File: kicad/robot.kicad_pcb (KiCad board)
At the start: 2 copper layers, 67.6 x 59.8 mm, 67 parts, among them J1 Adafruit Coil Jumper, J2 Adafruit Coil Jumper, J3 Adafruit Coil Jumper, J4 Adafruit Coil Jumper, M5 Motor_DC, M6 Motor_DC, M7 Motor_DC, M8 Motor_DC, Q2 NMOS, U10 GY-521, U13 DRV8833PW, U6 DRV8833PW, U8 ESP32-DEVKITC, U9 MCP73831-2-OT

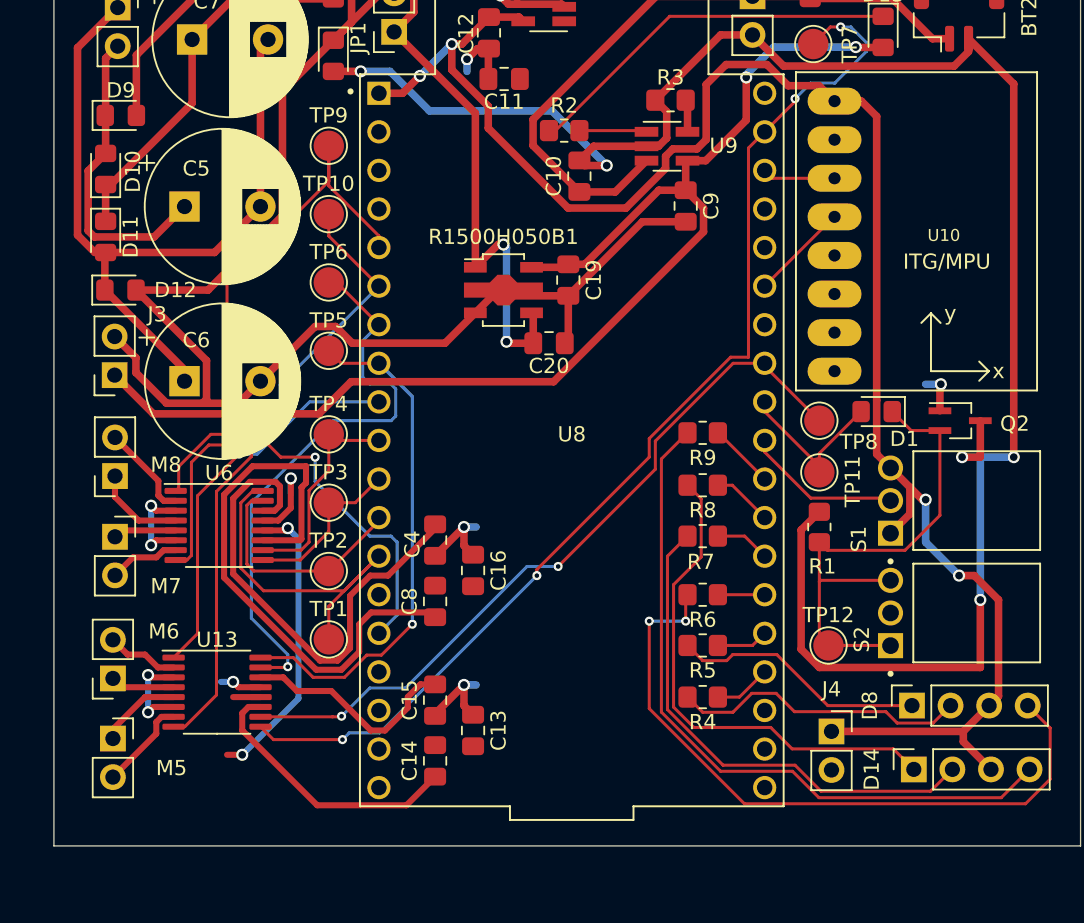
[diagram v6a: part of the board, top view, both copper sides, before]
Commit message: Add mounting holes
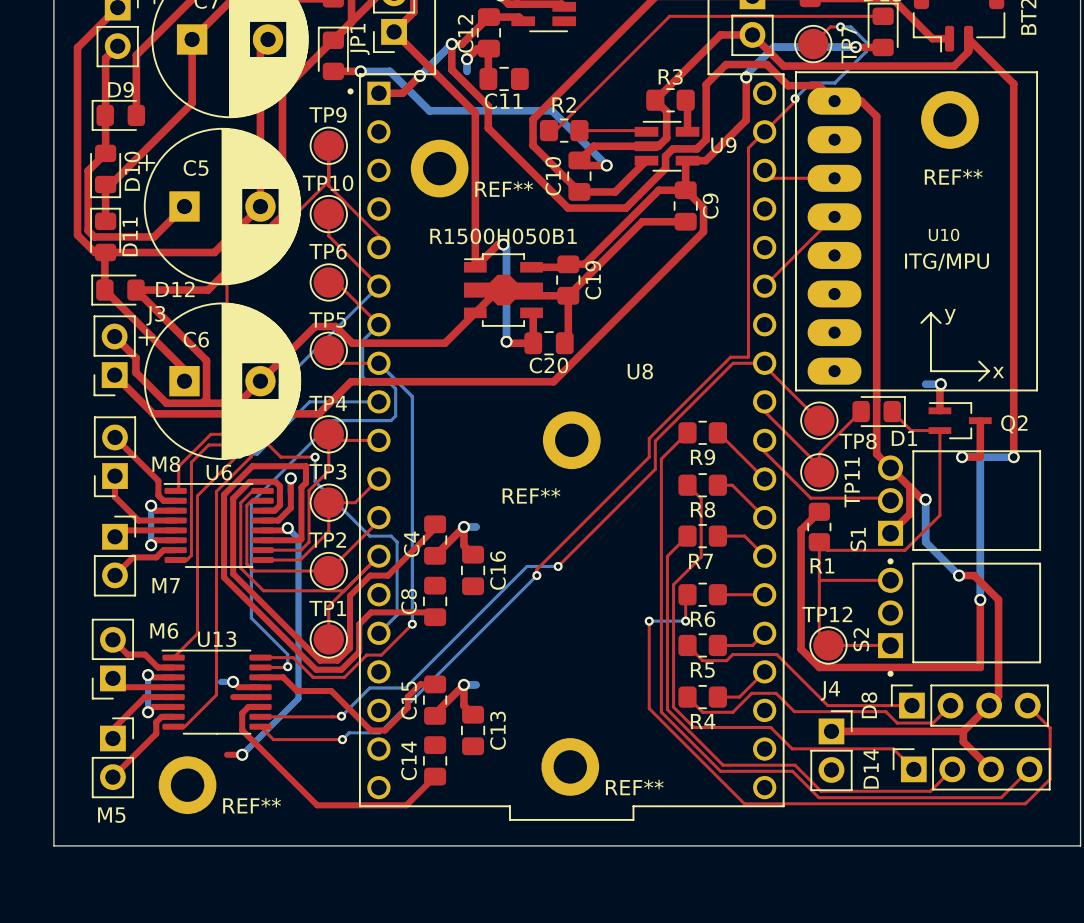
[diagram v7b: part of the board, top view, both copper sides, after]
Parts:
- added REF**: MountingHole_2.2mm_M2_DIN965_Pad, MountingHole:MountingHole_2.2mm_M2_DIN965_Pad, F.Cu at (181.8, 71.0)
- added REF**: MountingHole_2.2mm_M2_DIN965_Pad, MountingHole:MountingHole_2.2mm_M2_DIN965_Pad, F.Cu at (190.4, 110.4)
- added REF**: MountingHole_2.2mm_M2_DIN965_Pad, MountingHole:MountingHole_2.2mm_M2_DIN965_Pad, F.Cu at (215.4, 67.8)
- added REF**: MountingHole_2.2mm_M2_DIN965_Pad, MountingHole:MountingHole_2.2mm_M2_DIN965_Pad, F.Cu at (165.2, 111.6)
- added REF**: MountingHole_2.2mm_M2_DIN965_Pad, MountingHole:MountingHole_2.2mm_M2_DIN965_Pad, F.Cu at (190.5, 88.9)
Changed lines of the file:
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@@
       (net 39 "Net-(U13-nFAULT)") (pinfunction "1") (pintype "passive"))
   )
+  (footprint "MountingHole:MountingHole_2.2mm_M2_DIN965_Pad" (layer "F.Cu")
+    (at 181.8 71)
+    (descr "Mounting Hole 2.2mm, M2, DIN965")
+    (tags "mounting hole 2.2mm m2 din965")
+    (attr exclude_from_pos_files exclude_from_bom)
+    (fp_text reference "REF**" (at 4.2 1.4) (layer "F.SilkS")
+        (effects (font (size 1 1) (thickness 0.15)))
+    )
+    (fp_text value "MountingHole_2.2mm_M2_DIN965_Pad" (at 0 2.9) (layer "F.Fab")
+        (effects (font (size 1 1) (thickness 0.15)))
+    )
+    (fp_text user "${REFERENCE}" (at 0 0) (layer "F.Fab")
+        (effects (font (size 1 1) (thickness 0.15)))
+    )
+    (fp_circle (center 0 0) (end 1.9 0)
+      (stroke (width 0.15) (type solid)) (fill none) (layer "Cmts.User"))
+    (fp_circle (center 0 0) (end 2.15 0)
+      (stroke (width 0.05) (type solid)) (fill none) (layer "F.CrtYd"))
+    (pad "1" thru_hole circle (at 0 0) (size 3.8 3.8) (drill 2.2) (layers "*.Cu" "*.Mask"))
+  )
   (footprint "Connector_PinSocket_2.54mm:PinSocket_1x02_P2.54mm_Vertical" (layer "F.Cu")
     (at 160.6 60.4)
@@
     )
   )
+  (footprint "MountingHole:MountingHole_2.2mm_M2_DIN965_Pad" (layer "F.Cu")
+    (at 190.4 110.4)
+    (descr "Mounting Hole 2.2mm, M2, DIN965")
+    (tags "mounting hole 2.2mm m2 din965")
+    (attr exclude_from_pos_files exclude_from_bom)
+    (fp_text reference "REF**" (at 4.2 1.4) (layer "F.SilkS")
+        (effects (font (size 1 1) (thickness 0.15)))
+    )
+    (fp_text value "MountingHole_2.2mm_M2_DIN965_Pad" (at 0 2.9) (layer "F.Fab")
+        (effects (font (size 1 1) (thickness 0.15)))
+    )
+    (fp_text user "${REFERENCE}" (at 0 0) (layer "F.Fab")
+        (effects (font (size 1 1) (thickness 0.15)))
+    )
+    (fp_circle (center 0 0) (end 1.9 0)
+      (stroke (width 0.15) (type solid)) (fill none) (layer "Cmts.User"))
+    (fp_circle (center 0 0) (end 2.15 0)
+      (stroke (width 0.05) (type solid)) (fill none) (layer "F.CrtYd"))
+    (pad "1" thru_hole circle (at 0 0) (size 3.8 3.8) (drill 2.2) (layers "*.Cu" "*.Mask"))
+  )
   (footprint "Connector_PinSocket_2.54mm:PinSocket_1x02_P2.54mm_Vertical" (layer "F.Cu")
     (at 160.285 104.57 180)
@@
     (property "ki_keywords" "DC Motor")
     (attr through_hole)
-    (fp_text reference "M5" (at 3.8575 1.945) (layer "F.SilkS")
+    (fp_text reference "M5" (at -0.085 5.07) (layer "F.SilkS")
         (effects (font (size 1 1) (thickness 0.15)))
     )
@@
       (net 35 "Net-(U6-BIN2)") (pinfunction "1") (pintype "passive"))
   )
+  (footprint "MountingHole:MountingHole_2.2mm_M2_DIN965_Pad" (layer "F.Cu")
+    (at 215.4 67.8)
+    (descr "Mounting Hole 2.2mm, M2, DIN965")
+    (tags "mounting hole 2.2mm m2 din965")
+    (attr exclude_from_pos_files exclude_from_bom)
+    (fp_text reference "REF**" (at 0.2 3.8) (layer "F.SilkS")
+        (effects (font (size 1 1) (thickness 0.15)))
+    )
+    (fp_text value "MountingHole_2.2mm_M2_DIN965_Pad" (at 0 2.9) (layer "F.Fab")
+        (effects (font (size 1 1) (thickness 0.15)))
+    )
+    (fp_text user "${REFERENCE}" (at 0 0) (layer "F.Fab")
+        (effects (font (size 1 1) (thickness 0.15)))
+    )
+    (fp_circle (center 0 0) (end 1.9 0)
+      (stroke (width 0.15) (type solid)) (fill none) (layer "Cmts.User"))
+    (fp_circle (center 0 0) (end 2.15 0)
+      (stroke (width 0.05) (type solid)) (fill none) (layer "F.CrtYd"))
+    (pad "1" thru_hole circle (at 0 0) (size 3.8 3.8) (drill 2.2) (layers "*.Cu" "*.Mask"))
+  )
   (footprint "Capacitor_SMD:C_0805_2012Metric_Pad1.18x1.45mm_HandSolder" (layer "F.Cu")
     (at 184 97.4625 -90)
@@
     )
   )
+  (footprint "MountingHole:MountingHole_2.2mm_M2_DIN965_Pad" (layer "F.Cu")
+    (at 165.2 111.6)
+    (descr "Mounting Hole 2.2mm, M2, DIN965")
+    (tags "mounting hole 2.2mm m2 din965")
+    (attr exclude_from_pos_files exclude_from_bom)
+    (fp_text reference "REF**" (at 4.2 1.4) (layer "F.SilkS")
+        (effects (font (size 1 1) (thickness 0.15)))
+    )
+    (fp_text value "MountingHole_2.2mm_M2_DIN965_Pad" (at 0 2.9) (layer "F.Fab")
+        (effects (font (size 1 1) (thickness 0.15)))
+    )
+    (fp_text user "${REFERENCE}" (at 0 0) (layer "F.Fab")
+        (effects (font (size 1 1) (thickness 0.15)))
+    )
+    (fp_circle (center 0 0) (end 1.9 0)
+      (stroke (width 0.15) (type solid)) (fill none) (layer "Cmts.User"))
+    (fp_circle (center 0 0) (end 2.15 0)
+      (stroke (width 0.05) (type solid)) (fill none) (layer "F.CrtYd"))
+    (pad "1" thru_hole circle (at 0 0) (size 3.8 3.8) (drill 2.2) (layers "*.Cu" "*.Mask"))
+  )
   (footprint "Diode_SMD:D_0805_2012Metric_Pad1.15x1.40mm_HandSolder" (layer "F.Cu")
     (at 210.575 87 180)
@@
     (property "SnapEDA_Link" "https://www.snapeda.com/parts/ESP32-DEVKITC/Espressif+Systems/view-part/?ref=snap")
     (attr through_hole)
-    (fp_text reference "U8" (at 0 -0.39) (layer "F.SilkS")
+    (fp_text reference "U8" (at 4.5 -4.49) (layer "F.SilkS")
         (effects (font (size 1 1) (thickness 0.15)))
     )
@@
     )
   )
+  (footprint "MountingHole:MountingHole_2.2mm_M2_DIN965_Pad" (layer "F.Cu")
+    (at 190.5 88.89)
+    (descr "Mounting Hole 2.2mm, M2, DIN965")
+    (tags "mounting hole 2.2mm m2 din965")
+    (attr exclude_from_pos_files exclude_from_bom)
+    (fp_text reference "REF**" (at -2.7 3.71) (layer "F.SilkS")
+        (effects (font (size 1 1) (thickness 0.15)))
+    )
+    (fp_text value "MountingHole_2.2mm_M2_DIN965_Pad" (at 0 2.9) (layer "F.Fab")
+        (effects (font (size 1 1) (thickness 0.15)))
+    )
+    (fp_text user "${REFERENCE}" (at 0 0) (layer "F.Fab")
+        (effects (font (size 1 1) (thickness 0.15)))
+    )
+    (fp_circle (center 0 0) (end 1.9 0)
+      (stroke (width 0.15) (type solid)) (fill none) (layer "Cmts.User"))
+    (fp_circle (center 0 0) (end 2.15 0)
+      (stroke (width 0.05) (type solid)) (fill none) (layer "F.CrtYd"))
+    (pad "1" thru_hole circle (at 0 0) (size 3.8 3.8) (drill 2.2) (layers "*.Cu" "*.Mask"))
+  )
   (footprint "TestPoint:TestPoint_Pad_D2.0mm" (layer "F.Cu")

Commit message: Republish PCB footprint
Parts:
- removed REF**: MountingHole_2.2mm_M2_DIN965_Pad, MountingHole:MountingHole_2.2mm_M2_DIN965_Pad
- added R10: 10k, Resistor_SMD:R_0805_2012Metric_Pad1.20x1.40mm_HandSolder, F.Cu at (180.6, 69.2)
- added R11: 10k, Resistor_SMD:R_0805_2012Metric_Pad1.20x1.40mm_HandSolder, F.Cu at (180.6, 73.6)
- added R12: 10k, Resistor_SMD:R_0805_2012Metric_Pad1.20x1.40mm_HandSolder, F.Cu at (182.2, 87.8)
- added R13: 10k, Resistor_SMD:R_0805_2012Metric_Pad1.20x1.40mm_HandSolder, F.Cu at (184.6, 87.8)
- added R14: 10k, Resistor_SMD:R_0805_2012Metric_Pad1.20x1.40mm_HandSolder, F.Cu at (212.4, 83.2)
- R1: value 2k -> 10k
- moved REF1 0.08 mm to (190.5, 88.8)
- moved U8 0.08 mm to (190.5, 88.8)
- renumbered REF** to REF1, REF** to REF2, REF** to REF3, REF** to REF4
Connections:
- R5 pad 1: Net-(U8-IO2) -> Net-(U8-IO19)
- R6 pad 1: Net-(U8-IO0) -> Net-(U8-IO5)
- S1 pad 2: Net-(U8-IO5) -> Net-(U8-IO35)
- U8 pad 24: Net-(U8-IO2) -> Net-(U13-BIN2)
- U8 pad 25: Net-(U8-IO0) -> unconnected-(U8-IO0-Pad25)
- U8 pad 3: unconnected-(U8-SENSOR_VP-Pad3) -> Net-(U6-nFAULT)
- U8 pad 31: Net-(U13-BIN2) -> Net-(U8-IO19)
- U8 pad 4: unconnected-(U8-SENSOR_VN-Pad4) -> Net-(U13-nFAULT)
- U8 pad 5: Net-(U6-nFAULT) -> Net-(U8-IO34)
- U8 pad 6: Net-(U13-nFAULT) -> Net-(U8-IO35)
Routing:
- net Net-(U8-IO35): track 0.00 -> 50.6 mm, vias 0 -> 1
- net Net-(U8-IO19): track 0.00 -> 24.1 mm
- net Net-(U8-IO34): track 0.00 -> 15.4 mm, vias 0 -> 1
- net Net-(U13-BIN2): track 49.2 -> 58.0 mm
- net /Temporary/Controller/3V3: track 114.9 -> 123.1 mm
- net /Temporary/Controller/GND: track 44.4 -> 52.3 mm, vias 11 -> 12
- net Net-(U13-nFAULT): track 41.1 -> 45.1 mm, vias 1 -> 2
- net Net-(U8-IO5): track 10.4 -> 14.0 mm
- net Net-(U8-IO2): track 3.41 -> 0.00 mm
- net Net-(U8-IO0): track 3.08 -> 0.00 mm
- net Net-(U6-nFAULT): track 40.7 -> 39.4 mm
- net /Temporary/Controller/MOSTRIG: track 11.3 -> 12.5 mm
- net Net-(U13-BIN1): track 73.1 -> 72.4 mm
